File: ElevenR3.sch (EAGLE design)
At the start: 63 parts, among them IC1 ATMEGA328P, IC2 ATMEGA16U2-MU, IC3 MC33269DT-5.0, IC4 LM358D, IC5 LP2985-33DBVR, J1 Power, J2 Analog, J3 Digital_8_13, J4 Digital_0_7, J5 DC_2_1MM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

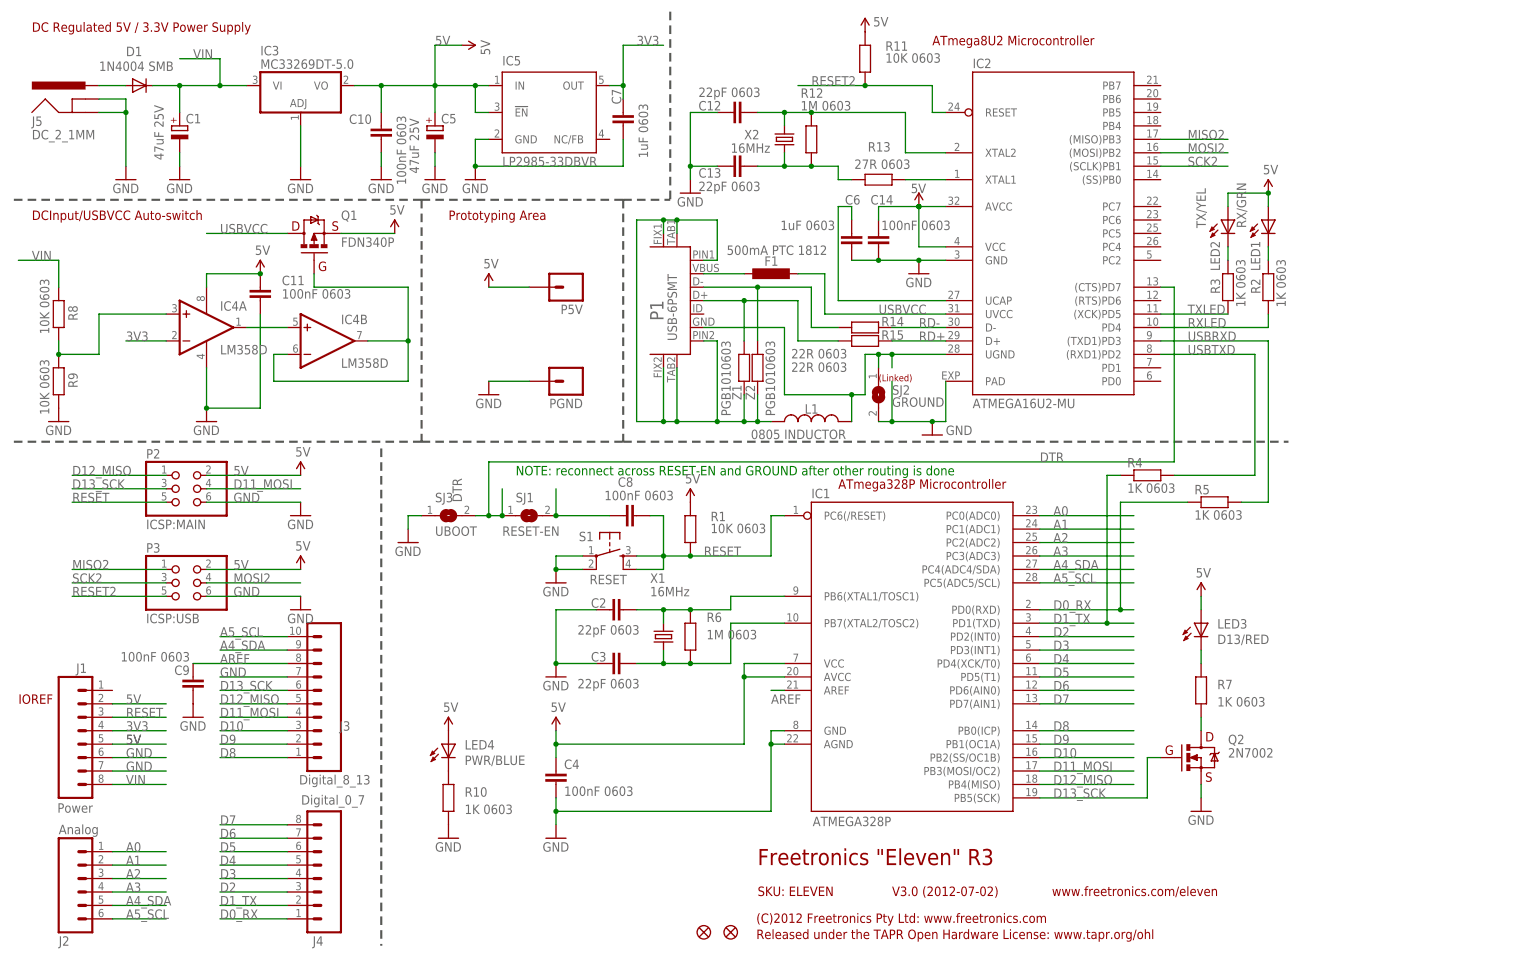
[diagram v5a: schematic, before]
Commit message: Replaced most parts using SuperHouse library to add 3D models
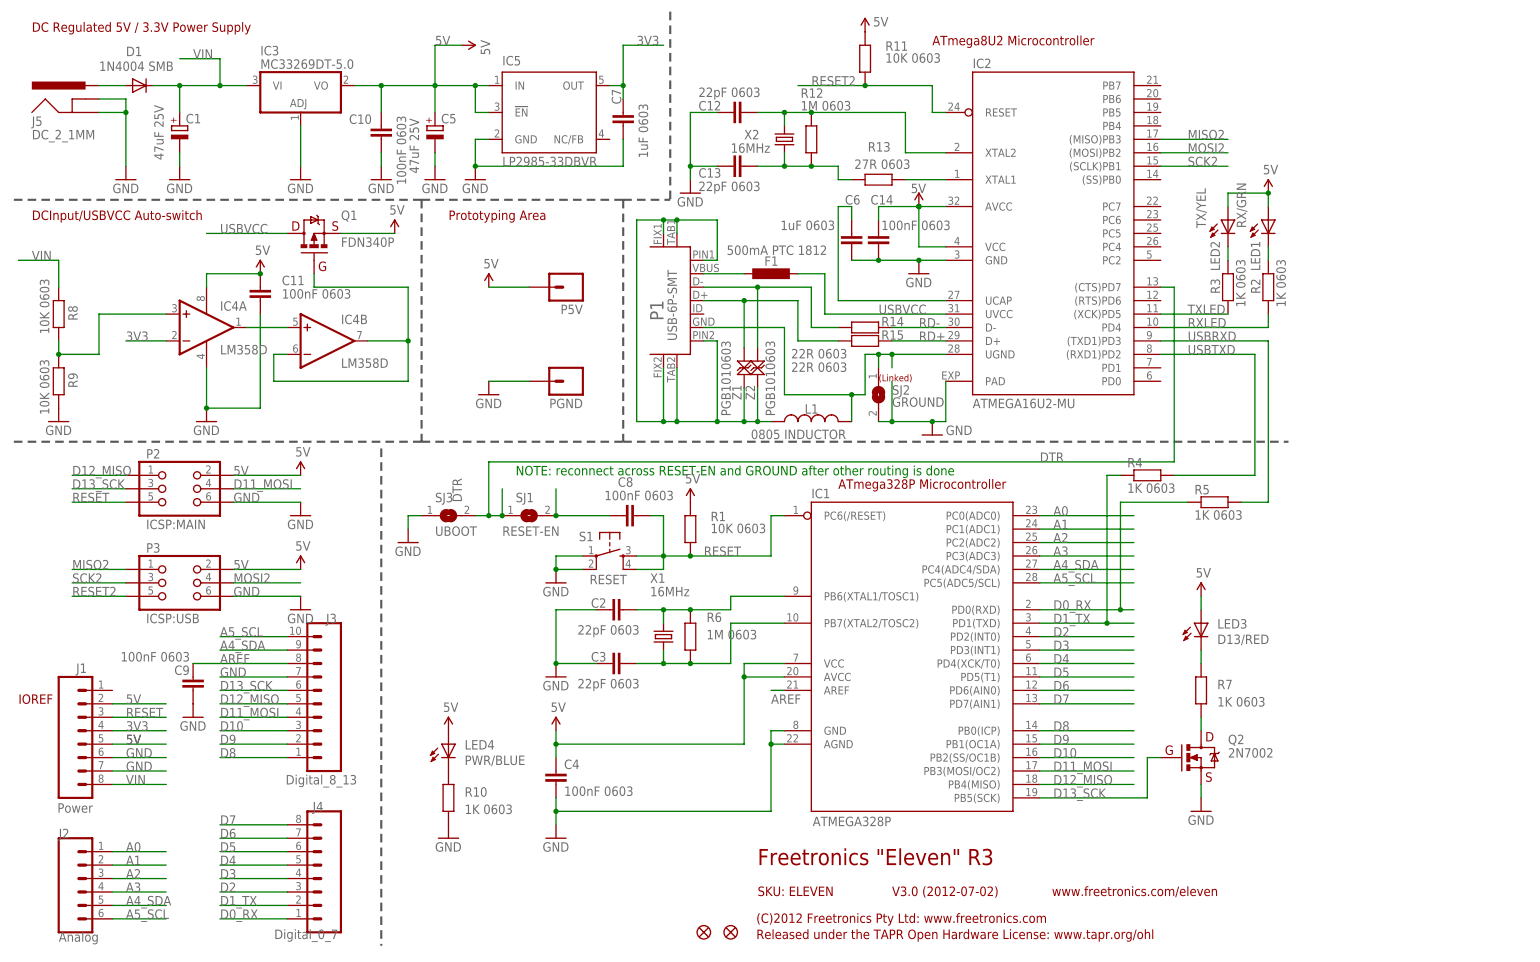
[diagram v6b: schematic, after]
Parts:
- C10, C11, C12, C13, C14, C2, C3, C4, C6, C7, C8, C9: device freetronics:CAP0603 -> SuperHouse-DiscreteSemi:CAP0603
- D1: device freetronics:DIODESMB -> SuperHouse-DiscreteSemi:DIODESMA
- IC1: device freetronics:AVR-MEGA8-P -> SuperHouse-MCUs:AVR-MEGA8-P
- IC2: device freetronics-jon:ATMEL_ATMEGA8U2-MUQFN -> SuperHouse-MCUs:ATMEGA8U2QFN
- IC3: device linear:MC33269D-5.0 -> SuperHouse-Regulators:MC33269-X-5.0-D
- IC4: device linear:LM358D -> SuperHouse-ICs:LM358D
- IC5: device freetronics-jon:TEXAS_TPS77033 -> SuperHouse-Regulators:LP2985-XX33
- J1, J4: device freetronics:M08 -> SuperHouse-Connectors:M08-SOCKET
- J2: device freetronics:M06SIP -> SuperHouse-Connectors:M06-SOCKET
- J3: device freetronics-original:M100.1 -> SuperHouse-Connectors:M10-SOCKET
- J5: device freetronics:POWER_JACKPTH -> SuperHouse-Connectors:POWER_JACK-SLOTS
- L1: device freetronics-master-v1:INDUCTOR0805-LARGE -> SuperHouse-DiscreteSemi:INDUCTOR0805-LARGE
- LED1, LED2, LED3, LED4: device freetronics:LED0603 -> SuperHouse-LEDs:LED0603
- P1: value USB-6PSMT -> USB-6P-SMT; device freetronics-jon:USB-6PSMT -> SuperHouse-Connectors:USB-6P-SMT
- P2, P3: device pinhead:PINHD-2X3 -> SuperHouse-Connectors:ICSPPTH
- Q1: device freetronics-master-v1:MOSFET-PCHANNEL -> SuperHouse-DiscreteSemi:MOSFET-PCHANNEL-SMT
- Q2: device freetronics:MOSFET-NCHANNELSMD -> SuperHouse-DiscreteSemi:MOSFET-NCHANNELSMD
- R1, R10, R11, R12, R13, R14, R15, R2, R3, R4, R5, R6, R7, R8, R9: device freetronics:RESISTOR0603 -> SuperHouse-DiscreteSemi:RESISTOR0603
- S1: device freetronics:TAC_SWITCHSMD -> SuperHouse-Switches:TAC_SWITCH-SMT-6
- X1, X2: device freetronics-master-v1:CRYSTALHC49UV -> SuperHouse-Oscillators:CRYSTALHC49UV
- Z1, Z2: device freetronics:RESISTOR0603 -> SuperHouse-DiscreteSemi:TVS0603
